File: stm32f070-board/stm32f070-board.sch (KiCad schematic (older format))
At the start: 21 parts

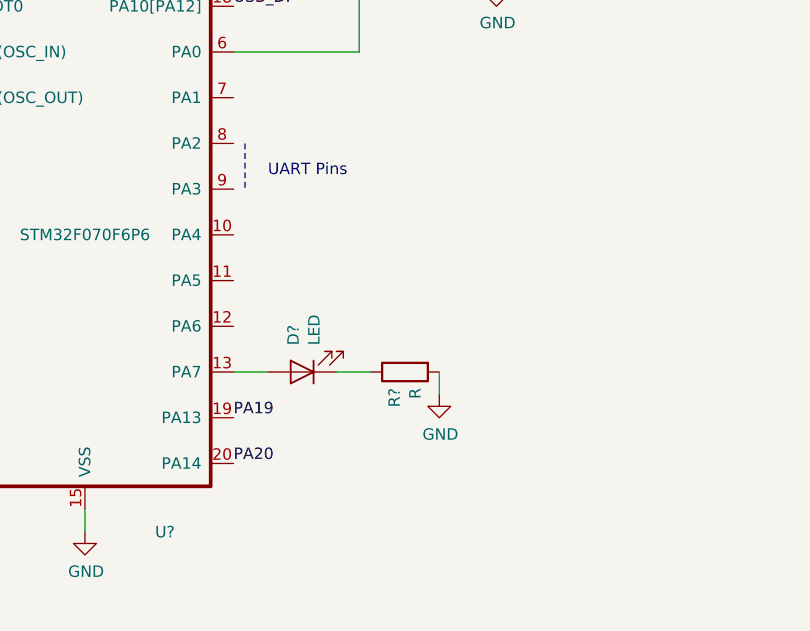
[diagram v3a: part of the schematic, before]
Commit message: created library for rgb led by modifying inbuild RGB led symbol and added rgb led to the main schematic.
Signed-off-by: suyash <in.suyash@gmail.com>
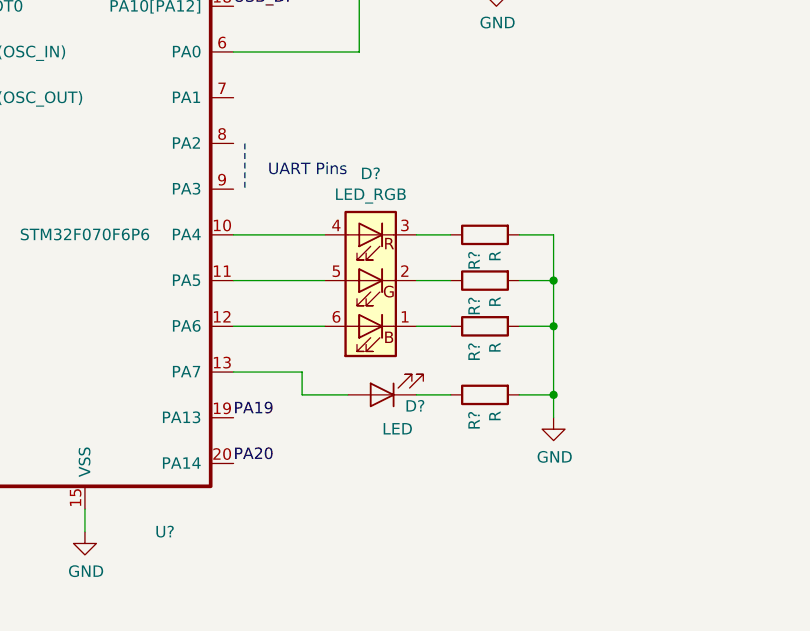
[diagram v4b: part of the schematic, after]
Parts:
- added D?: LED_RGB, symbol cree_rgb_led:LED_RGB
- added R? (x3): R, symbol Device:R
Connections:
- net GND: now also R?.2, R?.2, R?.2
- net at U?.10 (PA4): now also D?.4 (BA)
- net at U?.11 (PA5): now also D?.5 (GA)
- net at U?.12 (PA6): now also D?.6 (RA)
- new net: D?.1 (RK), R?.1
- new net: D?.2 (GK), R?.1
- new net: D?.3 (BK), R?.1
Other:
- moved on the sheet: D?, R?
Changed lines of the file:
@@
 L Device:LED D?
 U 1 1 5D7D3C44
-P 5650 5300
-F 0 "D?" V 5688 5183 50  0000 R CNN
-F 1 "LED" V 5597 5183 50  0000 R CNN
-F 2 "" H 5650 5300 50  0001 C CNN
-F 3 "~" H 5650 5300 50  0001 C CNN
-	1    5650 5300
+P 6000 5400
+F 0 "D?" H 5900 5450 50  0000 R CNN
+F 1 "LED" H 6000 5550 50  0000 R CNN
+F 2 "" H 6000 5400 50  0001 C CNN
+F 3 "~" H 6000 5400 50  0001 C CNN
+	1    6000 5400
 	-1   0    0    1
 $EndComp
@@
 L Device:R R?
 U 1 1 5D7D3F06
-P 6100 5300
-F 0 "R?" H 6170 5346 50  0000 L CNN
-F 1 "R" H 6170 5255 50  0000 L CNN
-F 2 "" V 6030 5300 50  0001 C CNN
-F 3 "~" H 6100 5300 50  0001 C CNN
-	1    6100 5300
+P 6450 5400
+F 0 "R?" H 6520 5446 50  0000 L CNN
+F 1 "R" H 6520 5355 50  0000 L CNN
+F 2 "" V 6380 5400 50  0001 C CNN
+F 3 "~" H 6450 5400 50  0001 C CNN
+	1    6450 5400
 	0    -1   1    0
 $EndComp
@@
 L power:GND #PWR?
 U 1 1 5D7D40BD
-P 6250 5400
-F 0 "#PWR?" H 6250 5150 50  0001 C CNN
-F 1 "GND" H 6255 5227 50  0000 C CNN
-F 2 "" H 6250 5400 50  0001 C CNN
-F 3 "" H 6250 5400 50  0001 C CNN
-	1    6250 5400
+P 6750 5500
+F 0 "#PWR?" H 6750 5250 50  0001 C CNN
+F 1 "GND" H 6755 5327 50  0000 C CNN
+F 2 "" H 6750 5500 50  0001 C CNN
+F 3 "" H 6750 5500 50  0001 C CNN
+	1    6750 5500
 	1    0    0    -1
 $EndComp
 Wire Wire Line
-	6250 5400 6250 5300
+	6300 5400 6150 5400
+$Comp
+L Device:R R?
+U 1 1 5D7D845C
+P 6450 5100
+F 0 "R?" H 6520 5146 50  0000 L CNN
+F 1 "R" H 6520 5055 50  0000 L CNN
+F 2 "" V 6380 5100 50  0001 C CNN
+F 3 "~" H 6450 5100 50  0001 C CNN
+	1    6450 5100
+	0    -1   1    0
+$EndComp
+$Comp
+L Device:R R?
+U 1 1 5D7D84B2
+P 6450 4900
+F 0 "R?" H 6520 4946 50  0000 L CNN
+F 1 "R" H 6520 4855 50  0000 L CNN
+F 2 "" V 6380 4900 50  0001 C CNN
+F 3 "~" H 6450 4900 50  0001 C CNN
+	1    6450 4900
+	0    -1   1    0
+$EndComp
+$Comp
+L Device:R R?
+U 1 1 5D7D84F8
+P 6450 4700
+F 0 "R?" H 6520 4746 50  0000 L CNN
+F 1 "R" H 6520 4655 50  0000 L CNN
+F 2 "" V 6380 4700 50  0001 C CNN
+F 3 "~" H 6450 4700 50  0001 C CNN
+	1    6450 4700
+	0    -1   1    0
+$EndComp
 Wire Wire Line
-	5950 5300 5800 5300
+	6600 5100 6750 5100
 Wire Wire Line
-	5500 5300 5350 5300
+	6600 4900 6750 4900
+Wire Wire Line
+	6750 4900 6750 5100
+Wire Wire Line
+	6600 4700 6750 4700
+Wire Wire Line
+	6750 4700 6750 4900
+Connection ~ 6750 4900
+Wire Wire Line
+	6750 5100 6750 5400
+Wire Wire Line
+	6750 5400 6600 5400
+Connection ~ 6750 5100
+Wire Wire Line
+	6750 5500 6750 5400
+Connection ~ 6750 5400
+Wire Wire Line
+	5350 5300 5650 5300
+Wire Wire Line
+	5650 5300 5650 5400
+Wire Wire Line
+	5650 5400 5850 5400
+$Comp
+L cree_rgb_led:LED_RGB D?
+U 1 1 5D801829
+P 5950 4900
+F 0 "D?" H 5950 4433 50  0000 C CNN
+F 1 "LED_RGB" H 5950 4524 50  0000 C CNN
+F 2 "" H 5950 4850 50  0001 C CNN
+F 3 "~" H 5950 4850 50  0001 C CNN
+	1    5950 4900
+	-1   0    0    1
+$EndComp
+Wire Wire Line
+	5350 5100 5750 5100
+Wire Wire Line
+	5350 4900 5750 4900
+Wire Wire Line
+	5350 4700 5750 4700
+Wire Wire Line
+	6150 4700 6300 4700
+Wire Wire Line
+	6150 4900 6300 4900
+Wire Wire Line
+	6150 5100 6300 5100
 $EndSCHEMATC

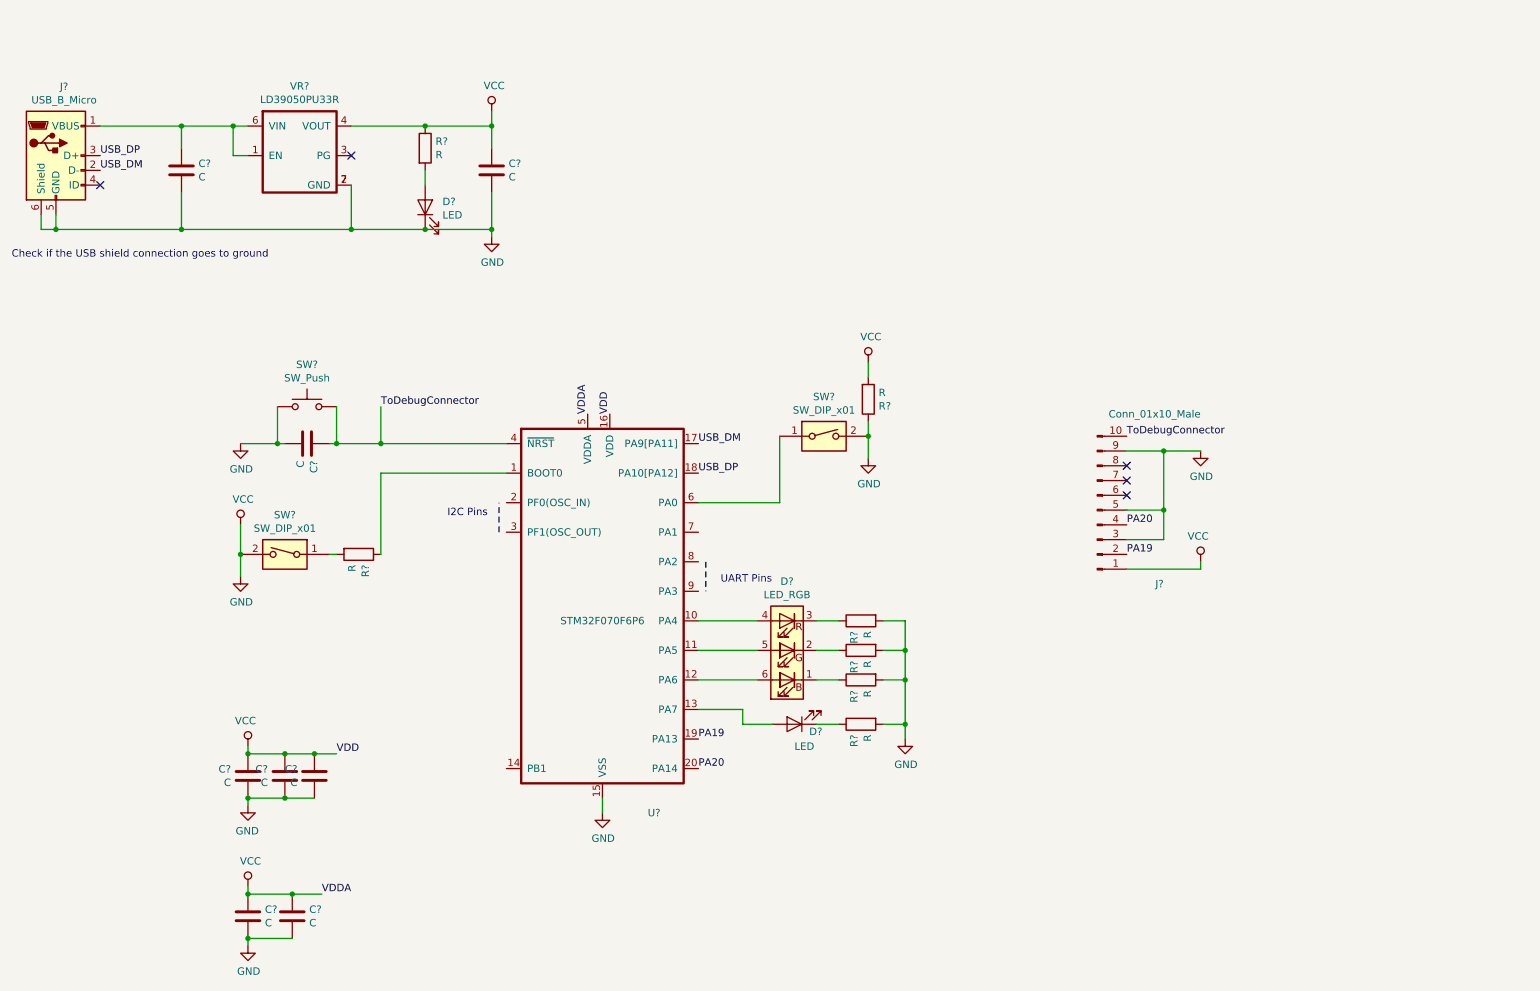
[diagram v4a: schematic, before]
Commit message: added temp sensors and ch340 to the schematic
Signed-off-by: suyash <in.suyash@gmail.com>
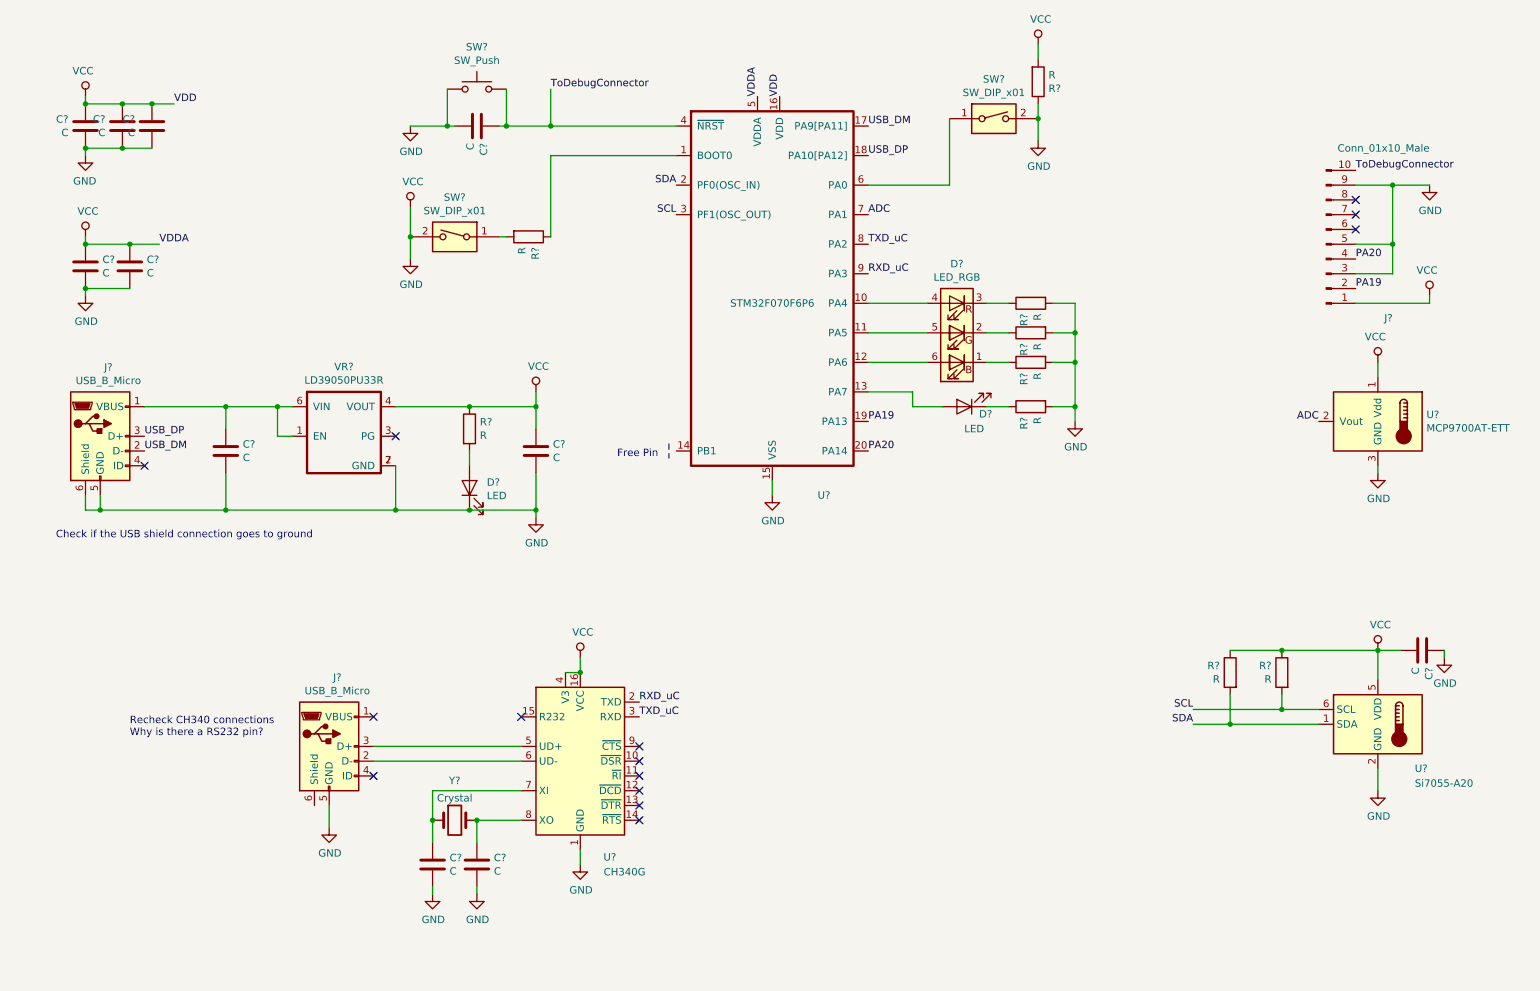
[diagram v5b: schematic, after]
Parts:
- added C? (x3): C, symbol Device:C
- added J?: USB_B_Micro, symbol Connector:USB_B_Micro
- added R? (x2): R, symbol Device:R
- added U?: MCP9700AT-ETT, Package_TO_SOT_SMD:SOT-23, symbol Sensor_Temperature:MCP9700AT-ETT
- added U?: Si7055-A20, Package_DFN_QFN:DFN-6-1EP_3x3mm_P1mm_EP1.65x2.55mm, symbol Sensor_Temperature:Si7055-A20
- added U?: CH340G, Package_SO:SOIC-16_3.9x9.9mm_P1.27mm, symbol Interface_USB:CH340G
- added Y?: Crystal, symbol Device:Crystal
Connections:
- net GND: now also C?.1, C?.2, C?.2, C?.2, J?.5 (GND), R?.1, R?.1, U?.1 (GND), U?.1 (Vdd), U?.16 (VCC), U?.2 (GND), U?.3 (GND), U?.4 (V3), U?.5 (VDD)
- net SDA: now reaches U?.2 (PF0(OSC_IN))
- net SDA: now also R?.2, U?.1 (SDA)
- net SCL: now reaches U?.3 (PF1(OSC_OUT))
- net SCL: now also R?.2, U?.6 (SCL)
- net ADC: now reaches U?.7 (PA1)
- net ADC: now also U?.2 (Vout)
- net TXD_uC: now reaches U?.8 (PA2)
- net TXD_uC: now also U?.3 (RXD)
- net RXD_uC: now reaches U?.9 (PA3)
- net RXD_uC: now also U?.2 (TXD)
- new net: J?.3 (D+), U?.5 (UD+)
- new net: J?.2 (D-), U?.6 (UD-)
- new net: C?.1, U?.7 (XI), Y?.1
- new net: C?.1, U?.8 (XO), Y?.2
- no-connect marks 5 -> 14
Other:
- note added: "Free Pin\n"
- note added: "Recheck CH340 connections\nWhy is there a RS232 pin?\n\n\n"
- note removed: "I2C Pins\n"
- note removed: "UART Pins\n"
- moved on the sheet: C?, D?, J?, R?, SW?, U?, VR?

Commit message: removed short in boot selector(added a 3way switch) and added zero ohm resistor in the user button.
Signed-off-by: suyash <in.suyash@gmail.com>
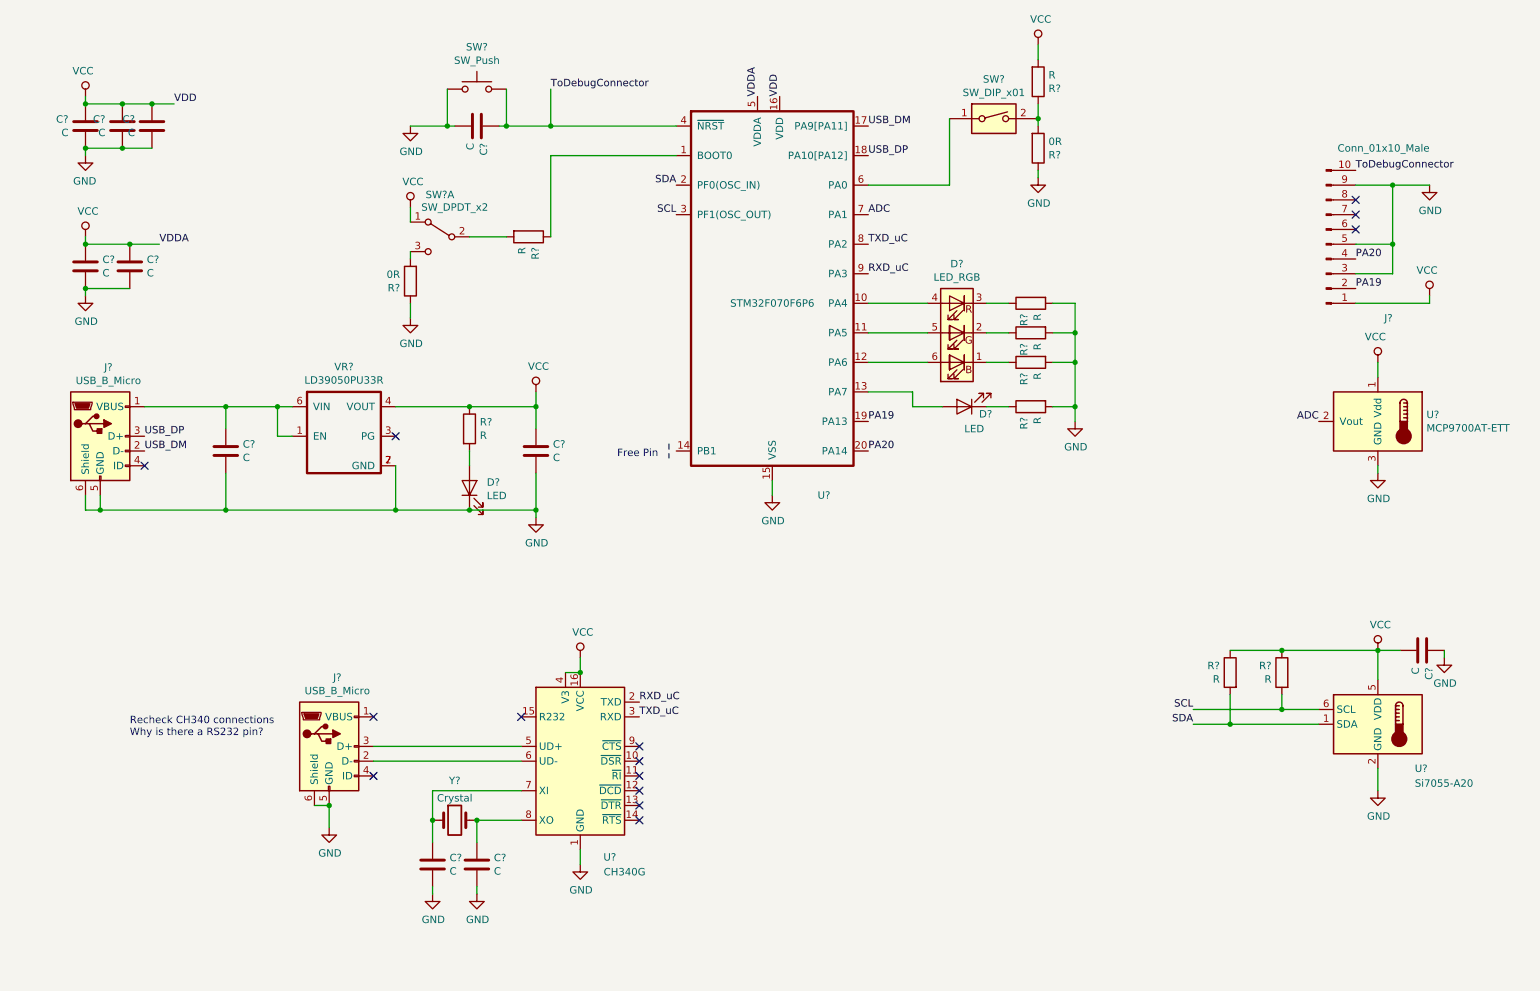
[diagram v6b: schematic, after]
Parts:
- removed SW?: SW_DIP_x01, symbol Switch:SW_DIP_x01
- added R? (x2): 0R, symbol Device:R
- added SW?: SW_DPDT_x2, symbol Switch:SW_DPDT_x2
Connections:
- net GND: now also J?.6 (Shield), R?.1, R?.1; no longer C?.1, C?.1, C?.1, C?.1, C?.1, C?.1, C?.2, J?.1 (Pin_1), R?.1, R?.1, R?.1, R?.1, R?.2, SW?.2, U?.1 (Vdd), U?.16 (VCC), U?.16 (VDD), U?.4 (V3), U?.5 (VDD), U?.5 (VDDA), VR?.4 (VOUT)
- net at R?.2: now also SW?.2 (B)
- new net: R?.1, R?.2, SW?.2
- new net: R?.2, SW?.3 (C)
- new net VCC: C?.1, C?.1, C?.1, C?.1, C?.1, C?.1, C?.2, J?.1 (Pin_1), R?.1, R?.1, R?.1, R?.2, SW?.1 (A), U?.1 (Vdd), U?.16 (VCC), U?.16 (VDD), U?.4 (V3), U?.5 (VDD), U?.5 (VDDA), VR?.4 (VOUT)
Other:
- note removed: "Check if the USB shield connection goes to ground\n"
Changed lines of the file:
@@
 	1200 3950 1300 3950
 Connection ~ 1300 3950
-Text Notes 1000 4150 0    50   ~ 0
-Check if the USB shield connection goes to ground\n
 NoConn ~ 3300 3450
 $Comp
@@
 L power:GND #PWR?
 U 1 1 5D7A7760
-P 3400 2250
-F 0 "#PWR?" H 3400 2000 50  0001 C CNN
-F 1 "GND" H 3405 2077 50  0000 C CNN
-F 2 "" H 3400 2250 50  0001 C CNN
-F 3 "" H 3400 2250 50  0001 C CNN
-	1    3400 2250
+P 3400 2650
+F 0 "#PWR?" H 3400 2400 50  0001 C CNN
+F 1 "GND" H 3405 2477 50  0000 C CNN
+F 2 "" H 3400 2650 50  0001 C CNN
+F 3 "" H 3400 2650 50  0001 C CNN
+	1    3400 2650
 	1    0    0    -1
 $EndComp
@@
 	0    1    1    0
 $EndComp
-$Comp
-L Switch:SW_DIP_x01 SW?
-U 1 1 5D7A7B4F
-P 3700 2100
-F 0 "SW?" H 3700 2367 50  0000 C CNN
-F 1 "SW_DIP_x01" H 3700 2276 50  0000 C CNN
-F 2 "" H 3700 2100 50  0001 C CNN
-F 3 "" H 3700 2100 50  0001 C CNN
-	1    3700 2100
-	-1   0    0    -1
-$EndComp
-Wire Wire Line
-	4000 2100 4050 2100
-Wire Wire Line
-	3400 2100 3400 1900
-Wire Wire Line
-	3400 2250 3400 2100
-Connection ~ 3400 2100
 $Comp
 L Switch:SW_Push SW?
@@
 USB_DP
 $Comp
-L Switch:SW_DIP_x01 SW?
-U 1 1 5D7CAFC7
-P 7350 1300
-F 0 "SW?" H 7350 1567 50  0000 C CNN
-F 1 "SW_DIP_x01" H 7350 1476 50  0000 C CNN
-F 2 "" H 7350 1300 50  0001 C CNN
-F 3 "" H 7350 1300 50  0001 C CNN
-	1    7350 1300
-	1    0    0    -1
-$EndComp
-$Comp
 L power:VCC #PWR?
 U 1 1 5D7CB054
@@
 Wire Wire Line
 	7650 900  7650 800
-Wire Wire Line
-	7650 1300 7650 1200
 $Comp
 L power:GND #PWR?
 U 1 1 5D7CE5CC
-P 7650 1450
-F 0 "#PWR?" H 7650 1200 50  0001 C CNN
-F 1 "GND" H 7655 1277 50  0000 C CNN
-F 2 "" H 7650 1450 50  0001 C CNN
-F 3 "" H 7650 1450 50  0001 C CNN
-	1    7650 1450
-	1    0    0    -1
-$EndComp
-Wire Wire Line
-	7650 1450 7650 1300
-Connection ~ 7650 1300
+P 7650 1700
+F 0 "#PWR?" H 7650 1450 50  0001 C CNN
+F 1 "GND" H 7655 1527 50  0000 C CNN
+F 2 "" H 7650 1700 50  0001 C CNN
+F 3 "" H 7650 1700 50  0001 C CNN
+	1    7650 1700
+	1    0    0    -1
+$EndComp
 Wire Wire Line
 	6500 1750 7050 1750
@@
 	4450 5050 4550 5050
 Connection ~ 4550 5050
+Wire Wire Line
+	2750 5950 2850 5950
+Connection ~ 2850 5950
+Wire Wire Line
+	7650 1300 7650 1200
+$Comp
+L Switch:SW_DIP_x01 SW?
+U 1 1 5D7CAFC7
+P 7350 1300
+F 0 "SW?" H 7350 1567 50  0000 C CNN
+F 1 "SW_DIP_x01" H 7350 1476 50  0000 C CNN
+F 2 "" H 7350 1300 50  0001 C CNN
+F 3 "" H 7350 1300 50  0001 C CNN
+	1    7350 1300
+	1    0    0    -1
+$EndComp
+$Comp
+L Device:R R?
+U 1 1 5D7B88B1
+P 7650 1500
+F 0 "R?" H 7720 1546 50  0000 L CNN
+F 1 "0R" H 7720 1455 50  0000 L CNN
+F 2 "" V 7580 1500 50  0001 C CNN
+F 3 "~" H 7650 1500 50  0001 C CNN
+	1    7650 1500
+	1    0    0    1
+$EndComp
+Wire Wire Line
+	7650 1700 7650 1650
+Wire Wire Line
+	7650 1350 7650 1300
+Connection ~ 7650 1300
+$Comp
+L Switch:SW_DPDT_x2 SW?
+U 1 1 5D7BECF9
+P 3600 2100
+F 0 "SW?" H 3600 2385 50  0000 C CNN
+F 1 "SW_DPDT_x2" H 3500 2300 50  0000 C CNN
+F 2 "" H 3600 2100 50  0001 C CNN
+F 3 "" H 3600 2100 50  0001 C CNN
+	1    3600 2100
+	-1   0    0    -1
+$EndComp
+Wire Wire Line
+	3400 2000 3400 1900
+Wire Wire Line
+	3800 2100 4050 2100
+$Comp
+L Device:R R?
+U 1 1 5D7D0CB6
+P 3400 2400
+F 0 "R?" H 3470 2446 50  0000 L CNN
+F 1 "0R" H 3470 2355 50  0000 L CNN
+F 2 "" V 3330 2400 50  0001 C CNN
+F 3 "~" H 3400 2400 50  0001 C CNN
+	1    3400 2400
+	-1   0    0    1
+$EndComp
+Wire Wire Line
+	3400 2650 3400 2550
+Wire Wire Line
+	3400 2250 3400 2200
 $EndSCHEMATC
